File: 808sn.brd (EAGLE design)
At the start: 100 x 80 mm, 72 parts, among them IC1 TL072P, IC2 TL072P, Q1 BC546A, Q45 BC546A, Q46 BC556, Q47 BC546A, Q48 BC546A, Q49 BC546A

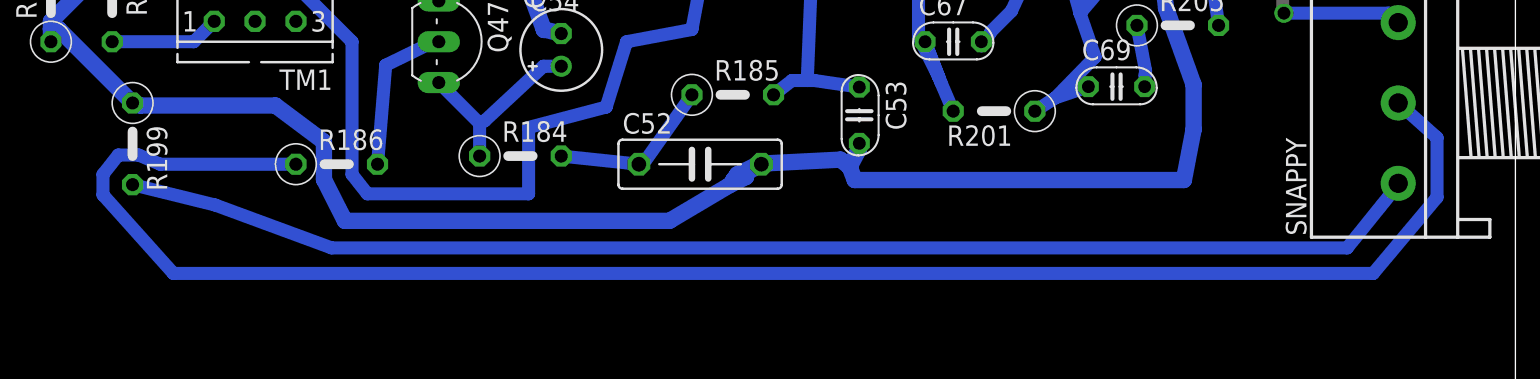
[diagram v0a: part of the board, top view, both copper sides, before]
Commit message: improved traces to snappy pot
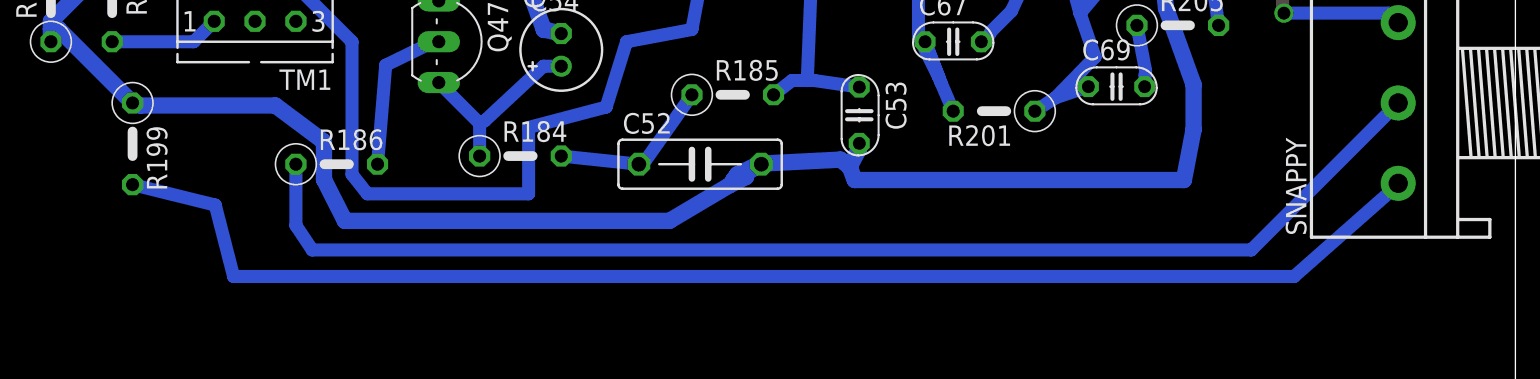
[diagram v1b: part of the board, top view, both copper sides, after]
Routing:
- net N$22: track 108.3 -> 77.0 mm
- net N$20: track 81.3 -> 84.6 mm
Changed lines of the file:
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@@
 <contactref element="R199" pad="2"/>
 <wire x1="19.1135" y1="16.51" x2="13.97" y2="17.78" width="0.8128" layer="16"/>
-<wire x1="26.3525" y1="13.843" x2="19.1135" y2="16.51" width="0.8128" layer="16"/>
-<wire x1="89.535" y1="13.843" x2="26.3525" y2="13.843" width="0.8128" layer="16"/>
-<wire x1="92.71" y1="17.78" x2="89.535" y2="13.843" width="0.8128" layer="16"/>
+<wire x1="20.2565" y1="12.065" x2="19.1135" y2="16.51" width="0.8128" layer="16"/>
+<wire x1="86.233" y1="12.065" x2="20.2565" y2="12.065" width="0.8128" layer="16"/>
+<wire x1="92.71" y1="17.78" x2="86.233" y2="12.065" width="0.8128" layer="16"/>
 <wire x1="92.71" y1="17.78" x2="92.71" y2="17.86" width="0.8128" layer="16"/>
 </signal>
@@
 <contactref element="SNAPPY" pad="2"/>
 <contactref element="R186" pad="1"/>
-<wire x1="15.6845" y1="19.05" x2="24.13" y2="19.05" width="0.8128" layer="16"/>
-<wire x1="14.351" y1="19.6215" x2="15.6845" y2="19.05" width="0.8128" layer="16"/>
-<wire x1="13.081" y1="19.6215" x2="14.351" y2="19.6215" width="0.8128" layer="16"/>
-<wire x1="12.1285" y1="18.415" x2="13.081" y2="19.6215" width="0.8128" layer="16"/>
-<wire x1="12.1285" y1="17.145" x2="12.1285" y2="18.415" width="0.8128" layer="16"/>
-<wire x1="16.51" y1="12.2555" x2="12.1285" y2="17.145" width="0.8128" layer="16"/>
-<wire x1="91.15425" y1="12.2555" x2="16.51" y2="12.2555" width="0.8128" layer="16"/>
-<wire x1="95.123" y1="16.98625" x2="91.15425" y2="12.2555" width="0.8128" layer="16"/>
-<wire x1="95.123" y1="20.701" x2="95.123" y2="16.98625" width="0.8128" layer="16"/>
-<wire x1="92.71" y1="22.86" x2="95.123" y2="20.701" width="0.8128" layer="16"/>
+<wire x1="24.13" y1="19.05" x2="24.13" y2="15.24" width="0.8128" layer="16"/>
+<wire x1="24.13" y1="15.24" x2="25.146" y2="13.716" width="0.8128" layer="16"/>
+<wire x1="25.146" y1="13.716" x2="83.566" y2="13.716" width="0.8128" layer="16"/>
+<wire x1="83.566" y1="13.716" x2="92.71" y2="22.86" width="0.8128" layer="16"/>
 </signal>
 <signal name="N$23">

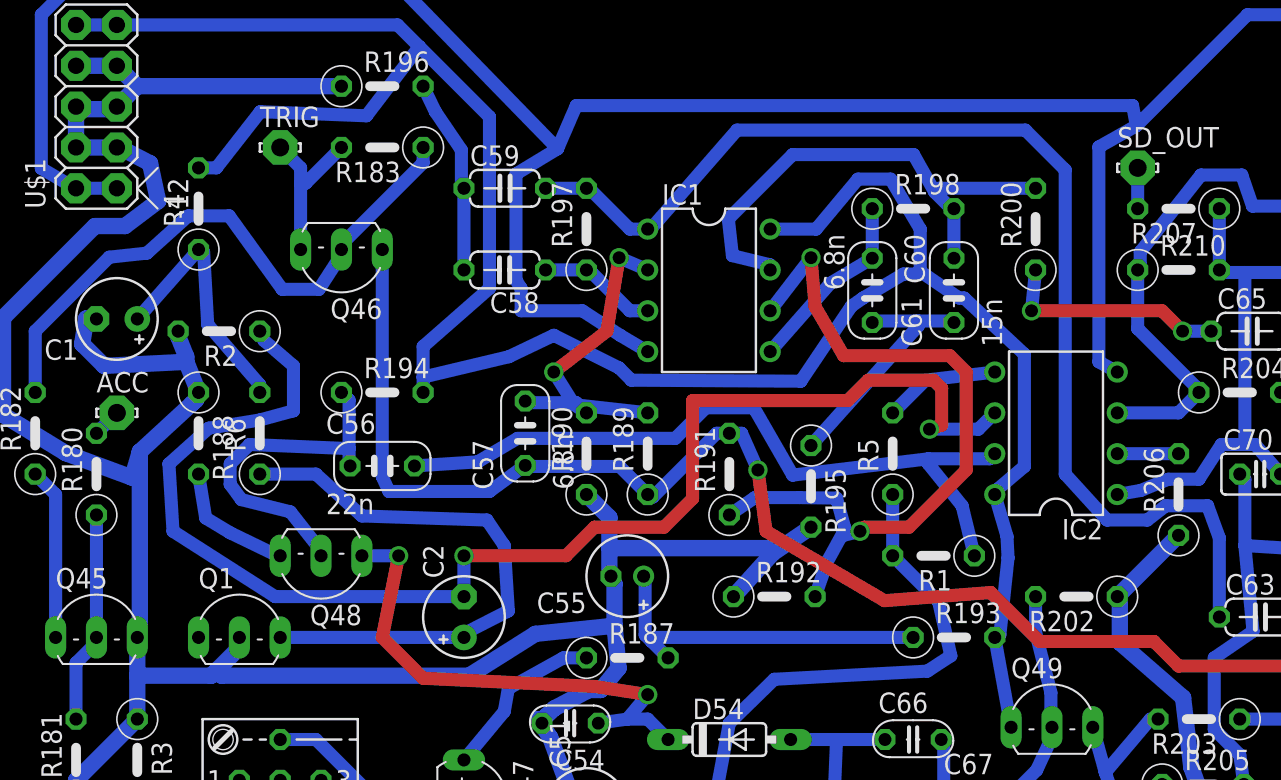
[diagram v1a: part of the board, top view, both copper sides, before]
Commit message: opamps flipped, working on layout
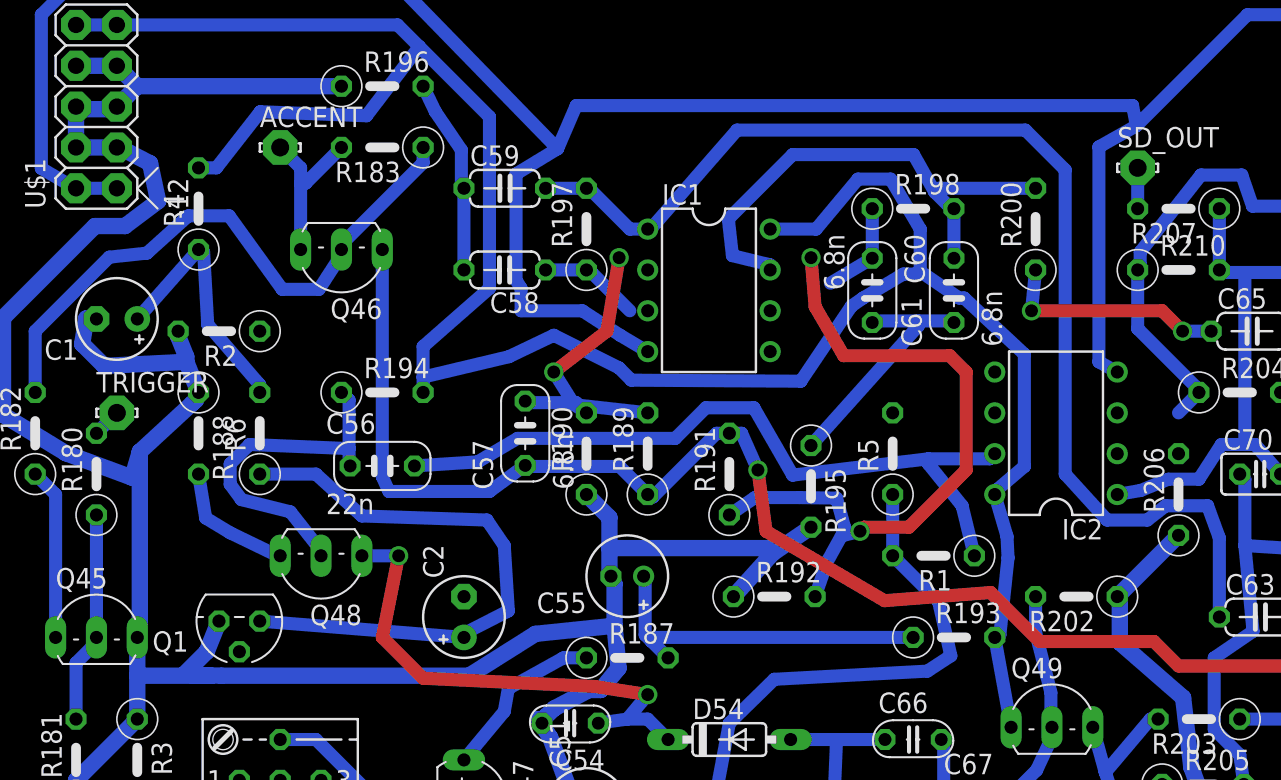
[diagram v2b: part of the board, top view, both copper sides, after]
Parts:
- C58: value 56n -> 27n
- C61: value 15n -> 6.8n
- Q1: value BC546A -> 2N3704; device transistor-npn:TO92-EBC -> transistor:TO92
- R191: value 10K -> 8.2K
- R3: value 47K -> 4.7K
- moved Q1 0.25 mm to (19.1, 37.8), turned to 180 degrees
- renumbered ACC to TRIGGER, TRIG to ACCENT
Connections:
- removed net N$53: IC2.2, R206.2
- removed net N$708: IC2.5, R5.2
- removed net N$712: C2.-, IC2.6, R2.1
- new net N$1: IC2.3, R206.2
- new net N$2: C2.-, IC2.5, R2.1
- new net N$3: IC2.6, R5.2
- net GND: now also Q1.1; no longer Q1.B
- net N$11: now also IC1.2; no longer IC1.3
- net N$16: now also IC1.5; no longer IC1.6
- net N$160: now also IC1.6; no longer IC1.5
- net N$35: now also IC2.2; no longer IC2.3
- net N$709: now also Q1.3; no longer Q1.E
- net N$8: now also IC1.3; no longer IC1.2
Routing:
- net N$712: track 86.2 -> 0.00 mm, vias 2 -> 0
- net N$708: track 7.22 -> 0.00 mm
- net N$160: track 11.8 -> 6.11 mm
- net GND: track 289.6 -> 294.1 mm
- net N$16: track 47.8 -> 43.7 mm
- net N$53: track 3.81 -> 0.00 mm
- net N$35: track 112.0 -> 108.2 mm
- net N$8: track 22.8 -> 20.9 mm
- net N$709: track 35.8 -> 37.2 mm
- net N$11: track 7.37 -> 6.26 mm
